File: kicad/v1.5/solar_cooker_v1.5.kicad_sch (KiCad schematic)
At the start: 17 parts, among them U10 GPS, U2 microSD, U3 clock_module, U5 anemometer, U6 BME680, U6 PT100, U7 pyranometer, U8 PT100, U9 AM2315, U9 PT100

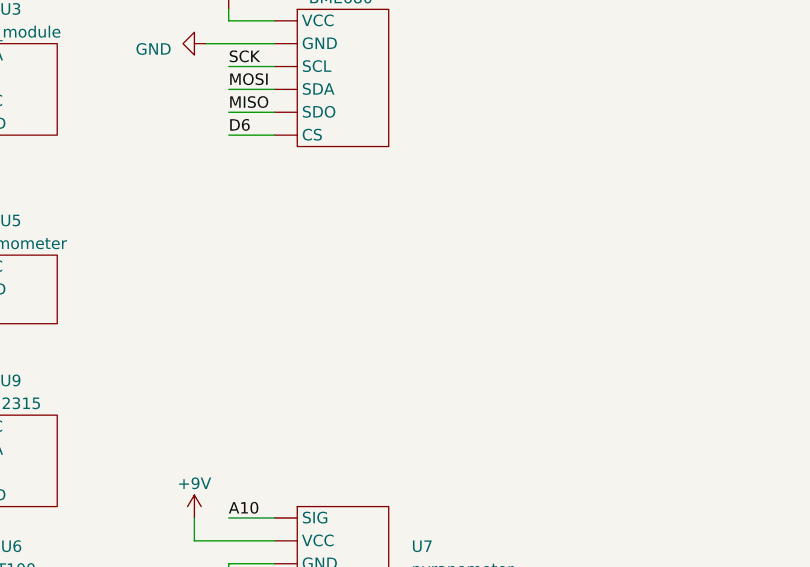
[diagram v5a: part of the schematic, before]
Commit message: added DC-DC converter
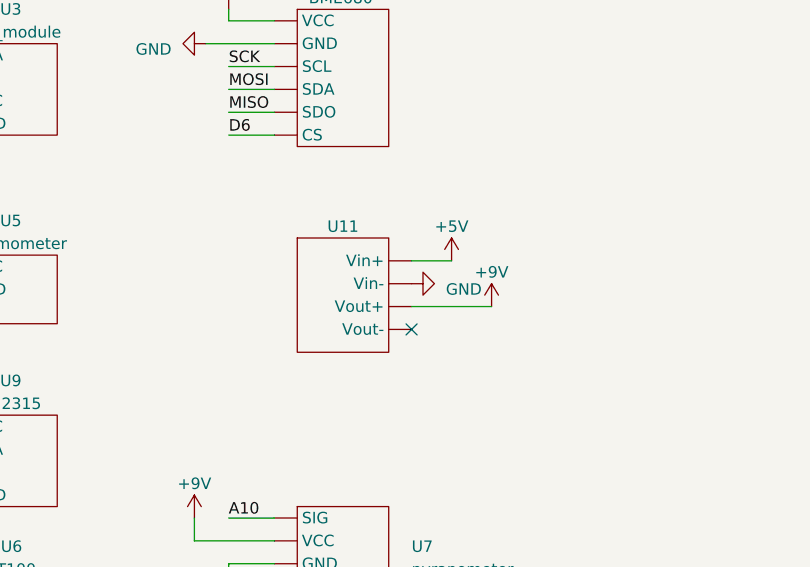
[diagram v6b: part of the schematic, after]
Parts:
- added U11: ~, symbol custom_components:converter
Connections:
- net +5V: now also U11. (Vout-)
- net +9V: now also U11. (Vout-)
- net GND: now also U11. (Vout-)
- no-connect marks 8 -> 9
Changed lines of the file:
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@@
   (junction (at 77.47 27.94) (diameter 0) (color 0 0 0 0)
   )
+  (no_connect (at 96.52 87.63))
   (no_connect (at 44.45 41.91))
   (no_connect (at 59.69 129.54))
@@
     (stroke (width 0) (type default) (color 0 0 255 1))
   )
+  (wire (pts (xy 96.52 85.09) (xy 105.41 85.09))
+    (stroke (width 0) (type default))
+  )
   (wire (pts (xy 59.69 124.46) (xy 64.77 124.46))
     (stroke (width 0) (type default) (color 0 0 255 1))
@@
   (wire (pts (xy 59.055 173.355) (xy 64.135 173.355))
     (stroke (width 0) (type default) (color 0 0 255 1))
+  )
+  (wire (pts (xy 96.52 80.01) (xy 100.965 80.01))
+    (stroke (width 0) (type default))
   )
   (wire (pts (xy 148.59 49.53) (xy 148.59 52.07))
@@
     )
   )
+  (symbol (lib_id "custom_components:converter") (at 88.9 76.2 0) (unit 1)
+    (in_bom yes) (on_board yes) (dnp no) (fields_autoplaced)
+    (property "Reference" "U11" (at 88.9 76.2 0)
+      (effects (font (size 1.27 1.27)))
+    )
+    (property "Value" "~" (at 88.9 76.2 0)
+      (effects (font (size 1.27 1.27)))
+    )
+    (property "Footprint" "" (at 88.9 76.2 0)
+      (effects (font (size 1.27 1.27)) hide)
+    )
+    (property "Datasheet" "" (at 88.9 76.2 0)
+      (effects (font (size 1.27 1.27)) hide)
+    )
+    (pin "")
+    (pin "")
+    (pin "")
+    (pin "")
+    (instances
+      (project "solar_cooker_v1.5"
+        (path "/c2c342ae-c172-4b44-a50e-ddd387eb2591"
+          (reference "U11") (unit 1)
+        )
+      )
+    )
+  )
   (symbol (lib_id "power:+5V") (at 63.5 191.135 0) (mirror x) (unit 1)
     (in_bom yes) (on_board yes) (dnp no) (fields_autoplaced)
@@
     )
   )
+  (symbol (lib_id "power:GND") (at 96.52 82.55 90) (unit 1)
+    (in_bom yes) (on_board yes) (dnp no) (fields_autoplaced)
+    (property "Reference" "#PWR028" (at 102.87 82.55 0)
+      (effects (font (size 1.27 1.27)) hide)
+    )
+    (property "Value" "GND" (at 100.33 83.185 90)
+      (effects (font (size 1.27 1.27)) (justify right))
+    )
+    (property "Footprint" "" (at 96.52 82.55 0)
+      (effects (font (size 1.27 1.27)) hide)
+    )
+    (property "Datasheet" "" (at 96.52 82.55 0)
+      (effects (font (size 1.27 1.27)) hide)
+    )
+    (pin "1")
+    (instances
+      (project "solar_cooker_v1.5"
+        (path "/c2c342ae-c172-4b44-a50e-ddd387eb2591"
+          (reference "#PWR028") (unit 1)
+        )
+      )
+    )
+  )
   (symbol (lib_id "power:GND") (at 164.465 59.69 0) (unit 1)
     (in_bom yes) (on_board yes) (dnp no)
@@
         (path "/c2c342ae-c172-4b44-a50e-ddd387eb2591"
           (reference "#PWR025") (unit 1)
+        )
+      )
+    )
+  )
+  (symbol (lib_id "power:+9V") (at 105.41 85.09 0) (unit 1)
+    (in_bom yes) (on_board yes) (dnp no) (fields_autoplaced)
+    (property "Reference" "#PWR017" (at 105.41 88.9 0)
+      (effects (font (size 1.27 1.27)) hide)
+    )
+    (property "Value" "+9V" (at 105.41 81.28 0)
+      (effects (font (size 1.27 1.27)))
+    )
+    (property "Footprint" "" (at 105.41 85.09 0)
+      (effects (font (size 1.27 1.27)) hide)
+    )
+    (property "Datasheet" "" (at 105.41 85.09 0)
+      (effects (font (size 1.27 1.27)) hide)
+    )
+    (pin "1")
+    (instances
+      (project "solar_cooker_v1.5"
+        (path "/c2c342ae-c172-4b44-a50e-ddd387eb2591"
+          (reference "#PWR017") (unit 1)
         )
       )
@@
         )
       )
+    )
+  )
+  (symbol (lib_id "power:+5V") (at 100.965 80.01 0) (unit 1)
+    (in_bom yes) (on_board yes) (dnp no) (fields_autoplaced)
+    (property "Reference" "#PWR018" (at 100.965 83.82 0)
+      (effects (font (size 1.27 1.27)) hide)
+    )
+    (property "Value" "+5V" (at 100.965 76.2 0)
+      (effects (font (size 1.27 1.27)))
+    )
+    (property "Footprint" "" (at 100.965 80.01 0)
+      (effects (font (size 1.27 1.27)) hide)
+    )
+    (property "Datasheet" "" (at 100.965 80.01 0)
+      (effects (font (size 1.27 1.27)) hide)
+    )
+    (pin "1")
+    (instances
+      (project "solar_cooker_v1.5"
+        (path "/c2c342ae-c172-4b44-a50e-ddd387eb2591"
+          (reference "#PWR018") (unit 1)
+        )
+      )

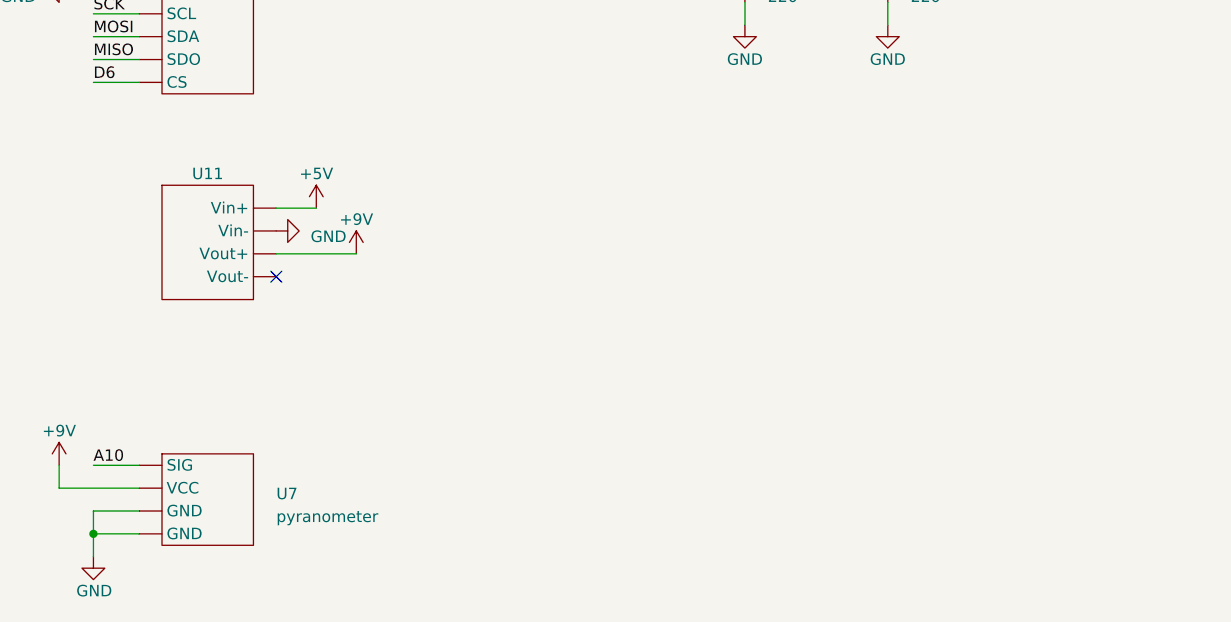
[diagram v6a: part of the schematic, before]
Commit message: converter scheme and footprint added
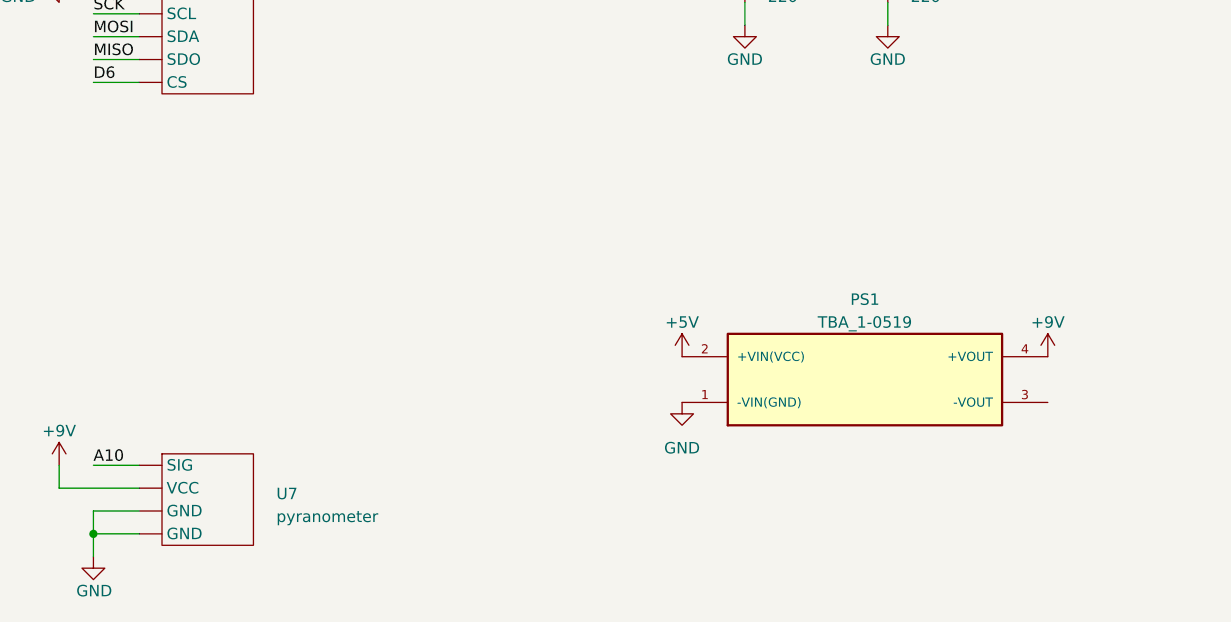
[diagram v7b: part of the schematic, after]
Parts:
- removed U11: ~, symbol custom_components:converter
- added PS1: TBA_1-0519, TBA_1-0519:CONV_TBA_1-0519, symbol TBA_1-0519:TBA_1-0519
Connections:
- net +5V: now also PS1.2 (+VIN(VCC))
- net +9V: now also PS1.4 (+VOUT)
- net GND: now also PS1.1 (-VIN(GND))
- no-connect marks 9 -> 8
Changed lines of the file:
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@@
   (junction (at 77.47 27.94) (diameter 0) (color 0 0 0 0)
   )
-  (no_connect (at 96.52 87.63))
   (no_connect (at 44.45 41.91))
   (no_connect (at 59.69 129.54))
@@
     (stroke (width 0) (type default) (color 0 0 255 1))
   )
-  (wire (pts (xy 96.52 85.09) (xy 105.41 85.09))
-    (stroke (width 0) (type default))
-  )
   (wire (pts (xy 59.69 124.46) (xy 64.77 124.46))
     (stroke (width 0) (type default) (color 0 0 255 1))
@@
   (wire (pts (xy 59.055 173.355) (xy 64.135 173.355))
     (stroke (width 0) (type default) (color 0 0 255 1))
-  )
-  (wire (pts (xy 96.52 80.01) (xy 100.965 80.01))
-    (stroke (width 0) (type default))
   )
   (wire (pts (xy 148.59 49.53) (xy 148.59 52.07))
@@
         (path "/c2c342ae-c172-4b44-a50e-ddd387eb2591"
           (reference "#PWR015") (unit 1)
+        )
+      )
+    )
+  )
+  (symbol (lib_id "power:+9V") (at 182.245 96.52 0) (unit 1)
+    (in_bom yes) (on_board yes) (dnp no) (fields_autoplaced)
+    (property "Reference" "#PWR031" (at 182.245 100.33 0)
+      (effects (font (size 1.27 1.27)) hide)
+    )
+    (property "Value" "+9V" (at 182.245 92.71 0)
+      (effects (font (size 1.27 1.27)))
+    )
+    (property "Footprint" "" (at 182.245 96.52 0)
+      (effects (font (size 1.27 1.27)) hide)
+    )
+    (property "Datasheet" "" (at 182.245 96.52 0)
+      (effects (font (size 1.27 1.27)) hide)
+    )
+    (pin "1")
+    (instances
+      (project "solar_cooker_v1.5"
+        (path "/c2c342ae-c172-4b44-a50e-ddd387eb2591"
+          (reference "#PWR031") (unit 1)
         )
       )
@@
     )
   )
+  (symbol (lib_id "power:+5V") (at 141.605 96.52 0) (unit 1)
+    (in_bom yes) (on_board yes) (dnp no) (fields_autoplaced)
+    (property "Reference" "#PWR029" (at 141.605 100.33 0)
+      (effects (font (size 1.27 1.27)) hide)
+    )
+    (property "Value" "+5V" (at 141.605 92.71 0)
+      (effects (font (size 1.27 1.27)))
+    )
+    (property "Footprint" "" (at 141.605 96.52 0)
+      (effects (font (size 1.27 1.27)) hide)
+    )
+    (property "Datasheet" "" (at 141.605 96.52 0)
+      (effects (font (size 1.27 1.27)) hide)
+    )
+    (pin "1")
+    (instances
+      (project "solar_cooker_v1.5"
+        (path "/c2c342ae-c172-4b44-a50e-ddd387eb2591"
+          (reference "#PWR029") (unit 1)
+        )
+      )
+    )
+  )
   (symbol (lib_id "Device:R_Small") (at 77.47 31.75 180) (unit 1)
     (in_bom yes) (on_board yes) (dnp no)
@@
     )
   )
-  (symbol (lib_id "custom_components:converter") (at 88.9 76.2 0) (unit 1)
-    (in_bom yes) (on_board yes) (dnp no) (fields_autoplaced)
-    (property "Reference" "U11" (at 88.9 76.2 0)
-      (effects (font (size 1.27 1.27)))
-    )
-    (property "Value" "~" (at 88.9 76.2 0)
-      (effects (font (size 1.27 1.27)))
-    )
-    (property "Footprint" "" (at 88.9 76.2 0)
-      (effects (font (size 1.27 1.27)) hide)
-    )
-    (property "Datasheet" "" (at 88.9 76.2 0)
-      (effects (font (size 1.27 1.27)) hide)
-    )
-    (pin "")
-    (pin "")
-    (pin "")
-    (pin "")
-    (instances
-      (project "solar_cooker_v1.5"
-        (path "/c2c342ae-c172-4b44-a50e-ddd387eb2591"
-          (reference "U11") (unit 1)
-        )
-      )
-    )
-  )
   (symbol (lib_id "power:+5V") (at 63.5 191.135 0) (mirror x) (unit 1)
     (in_bom yes) (on_board yes) (dnp no) (fields_autoplaced)
@@
     )
   )
-  (symbol (lib_id "power:GND") (at 96.52 82.55 90) (unit 1)
-    (in_bom yes) (on_board yes) (dnp no) (fields_autoplaced)
-    (property "Reference" "#PWR028" (at 102.87 82.55 0)
-      (effects (font (size 1.27 1.27)) hide)
-    )
-    (property "Value" "GND" (at 100.33 83.185 90)
-      (effects (font (size 1.27 1.27)) (justify right))
-    )
-    (property "Footprint" "" (at 96.52 82.55 0)
-      (effects (font (size 1.27 1.27)) hide)
-    )
-    (property "Datasheet" "" (at 96.52 82.55 0)
-      (effects (font (size 1.27 1.27)) hide)
-    )
-    (pin "1")
-    (instances
-      (project "solar_cooker_v1.5"
-        (path "/c2c342ae-c172-4b44-a50e-ddd387eb2591"
-          (reference "#PWR028") (unit 1)
-        )
-      )
-    )
-  )
   (symbol (lib_id "power:GND") (at 164.465 59.69 0) (unit 1)
     (in_bom yes) (on_board yes) (dnp no)
@@
         (path "/c2c342ae-c172-4b44-a50e-ddd387eb2591"
           (reference "#PWR025") (unit 1)
-        )
-      )
-    )
-  )
-  (symbol (lib_id "power:+9V") (at 105.41 85.09 0) (unit 1)
-    (in_bom yes) (on_board yes) (dnp no) (fields_autoplaced)
-    (property "Reference" "#PWR017" (at 105.41 88.9 0)
-      (effects (font (size 1.27 1.27)) hide)
-    )
-    (property "Value" "+9V" (at 105.41 81.28 0)
-      (effects (font (size 1.27 1.27)))
-    )
-    (property "Footprint" "" (at 105.41 85.09 0)
-      (effects (font (size 1.27 1.27)) hide)
-    )
-    (property "Datasheet" "" (at 105.41 85.09 0)
-      (effects (font (size 1.27 1.27)) hide)
-    )
-    (pin "1")
-    (instances
-      (project "solar_cooker_v1.5"
-        (path "/c2c342ae-c172-4b44-a50e-ddd387eb2591"
-          (reference "#PWR017") (unit 1)
         )
       )
@@
     )
   )
+  (symbol (lib_id "TBA_1-0519:TBA_1-0519") (at 161.925 99.06 0) (unit 1)
+    (in_bom yes) (on_board yes) (dnp no) (fields_autoplaced)
+    (property "Reference" "PS1" (at 161.925 90.17 0)
+      (effects (font (size 1.27 1.27)))
+    )
+    (property "Value" "TBA_1-0519" (at 161.925 92.71 0)
+      (effects (font (size 1.27 1.27)))
+    )
+    (property "Footprint" "TBA_1-0519:CONV_TBA_1-0519" (at 161.925 99.06 0)
+      (effects (font (size 1.27 1.27)) (justify bottom) hide)
+    )
+    (property "Datasheet" "" (at 161.925 99.06 0)
+      (effects (font (size 1.27 1.27)) hide)
+    )
+    (property "PARTREV" "April 19, 2021" (at 161.925 99.06 0)
+      (effects (font (size 1.27 1.27)) (justify bottom) hide)
+    )
+    (property "STANDARD" "Manufacturer Recommendations" (at 161.925 99.06 0)
+      (effects (font (size 1.27 1.27)) (justify bottom) hide)
+    )
+    (property "MAXIMUM_PACKAGE_HEIGHT" "10.15mm" (at 161.925 99.06 0)
+      (effects (font (size 1.27 1.27)) (justify bottom) hide)
+    )
+    (property "MANUFACTURER" "Traco Power" (at 161.925 99.06 0)
+      (effects (font (size 1.27 1.27)) (justify bottom) hide)
+    )
+    (pin "1")
+    (pin "2")
+    (pin "3")
+    (pin "4")
+    (instances
+      (project "solar_cooker_v1.5"
+        (path "/c2c342ae-c172-4b44-a50e-ddd387eb2591"
+          (reference "PS1") (unit 1)
+        )
+      )
+    )
+  )
   (symbol (lib_id "custom_components:GPS") (at 140.335 163.195 0) (unit 1)
     (in_bom yes) (on_board yes) (dnp no) (fields_autoplaced)
@@
     )
   )
+  (symbol (lib_id "power:GND") (at 141.605 101.6 0) (unit 1)
+    (in_bom yes) (on_board yes) (dnp no) (fields_autoplaced)
+    (property "Reference" "#PWR030" (at 141.605 107.95 0)
+      (effects (font (size 1.27 1.27)) hide)
+    )
+    (property "Value" "GND" (at 141.605 106.68 0)
+      (effects (font (size 1.27 1.27)))
+    )
+    (property "Footprint" "" (at 141.605 101.6 0)
+      (effects (font (size 1.27 1.27)) hide)
+    )
+    (property "Datasheet" "" (at 141.605 101.6 0)
+      (effects (font (size 1.27 1.27)) hide)
+    )
+    (pin "1")
+    (instances
+      (project "solar_cooker_v1.5"
+        (path "/c2c342ae-c172-4b44-a50e-ddd387eb2591"
+          (reference "#PWR030") (unit 1)
+        )
+      )
+    )
+  )
   (symbol (lib_id "custom_components:clock_module") (at 52.07 60.96 0) (unit 1)
     (in_bom yes) (on_board yes) (dnp no)
@@
         )
       )
-    )
-  )
-  (symbol (lib_id "power:+5V") (at 100.965 80.01 0) (unit 1)
-    (in_bom yes) (on_board yes) (dnp no) (fields_autoplaced)
-    (property "Reference" "#PWR018" (at 100.965 83.82 0)
-      (effects (font (size 1.27 1.27)) hide)
-    )
-    (property "Value" "+5V" (at 100.965 76.2 0)
-      (effects (font (size 1.27 1.27)))
-    )
-    (property "Footprint" "" (at 100.965 80.01 0)
-      (effects (font (size 1.27 1.27)) hide)
-    )
-    (property "Datasheet" "" (at 100.965 80.01 0)
-      (effects (font (size 1.27 1.27)) hide)
-    )
-    (pin "1")
-    (instances
-      (project "solar_cooker_v1.5"
-        (path "/c2c342ae-c172-4b44-a50e-ddd387eb2591"
-          (reference "#PWR018") (unit 1)
-        )
-      )

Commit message: drc fix
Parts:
- removed PS1: TBA_1-0519, TBA_1-0519:CONV_TBA_1-0519, symbol TBA_1-0519:TBA_1-0519
- added PS1: TBA_1-0519, dcdc convertor:CONV_TBA_1-0519, symbol dcdc convertor:TBA_1-0519
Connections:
- net +5V: now also A1.5V_3 (+5V_3), PS1.2 (+VIN(VCC))
- net +9V: now also PS1.4 (+VOUT)
- net GND: now also A1.GND2, A1.GND3, A1.GND4, A1.GND5, PS1.1 (-VIN(GND))
- no-connect marks 8 -> 74
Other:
- moved on the sheet: D?, R1, R?, S1, U10, U3, U5, U6, U7, U8, U9
